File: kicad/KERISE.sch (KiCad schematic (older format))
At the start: 5 parts, among them SW1 RESET, U1 ESP32-PICO-D4

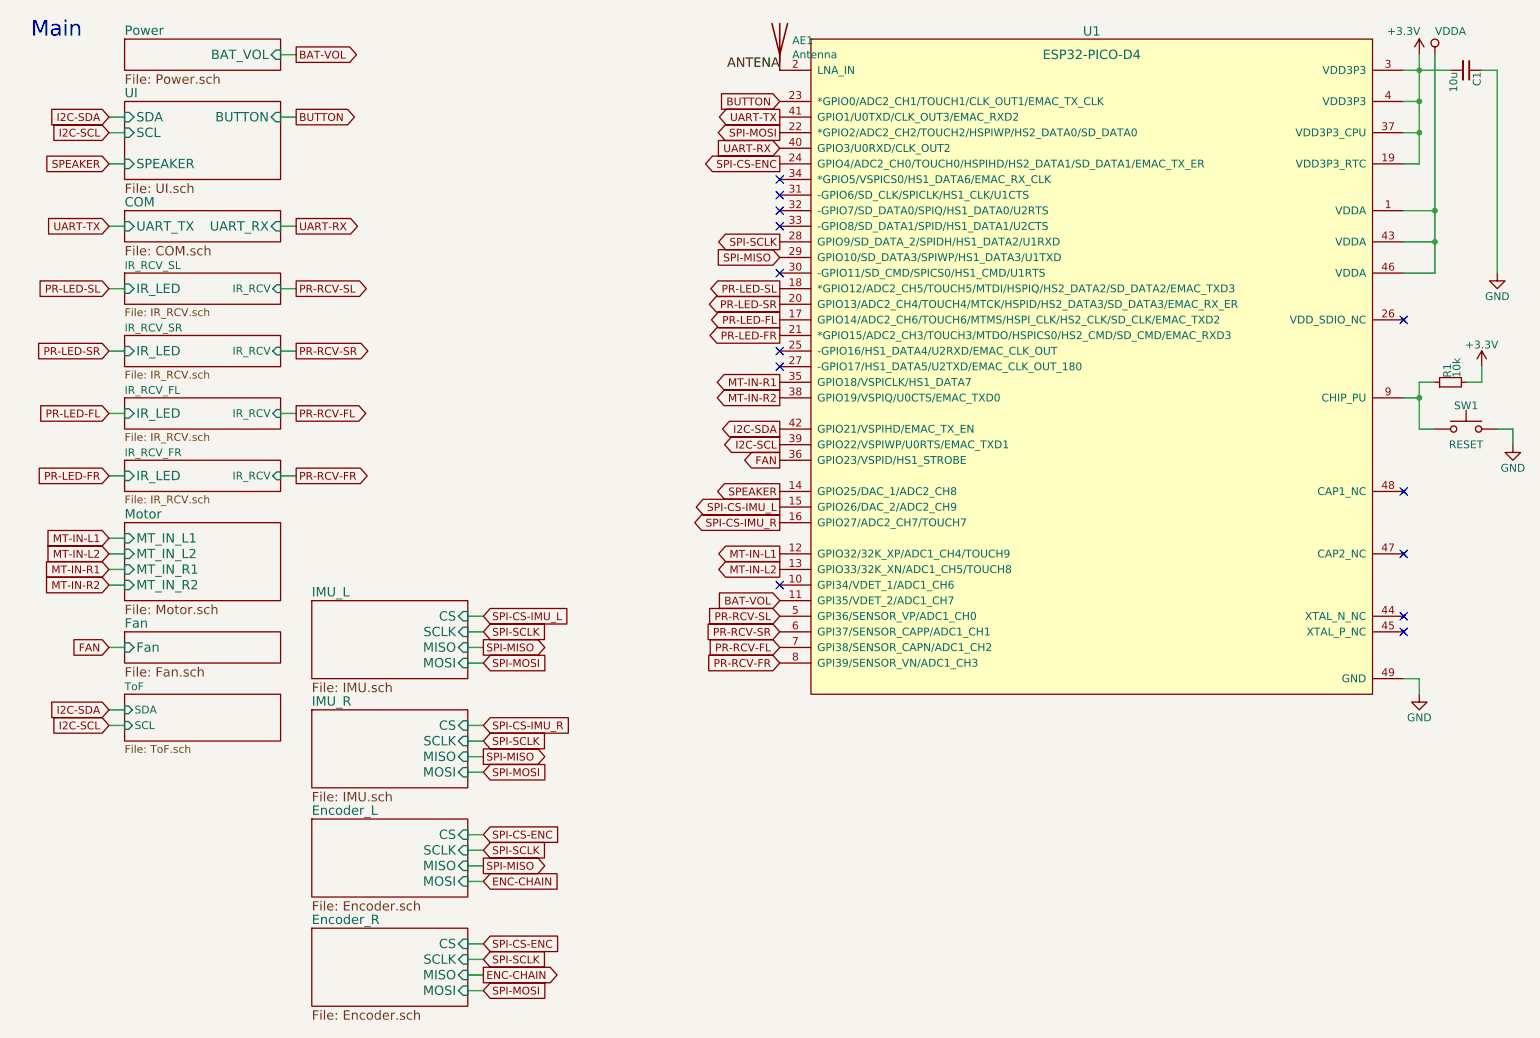
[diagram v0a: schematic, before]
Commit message: 部品を配置
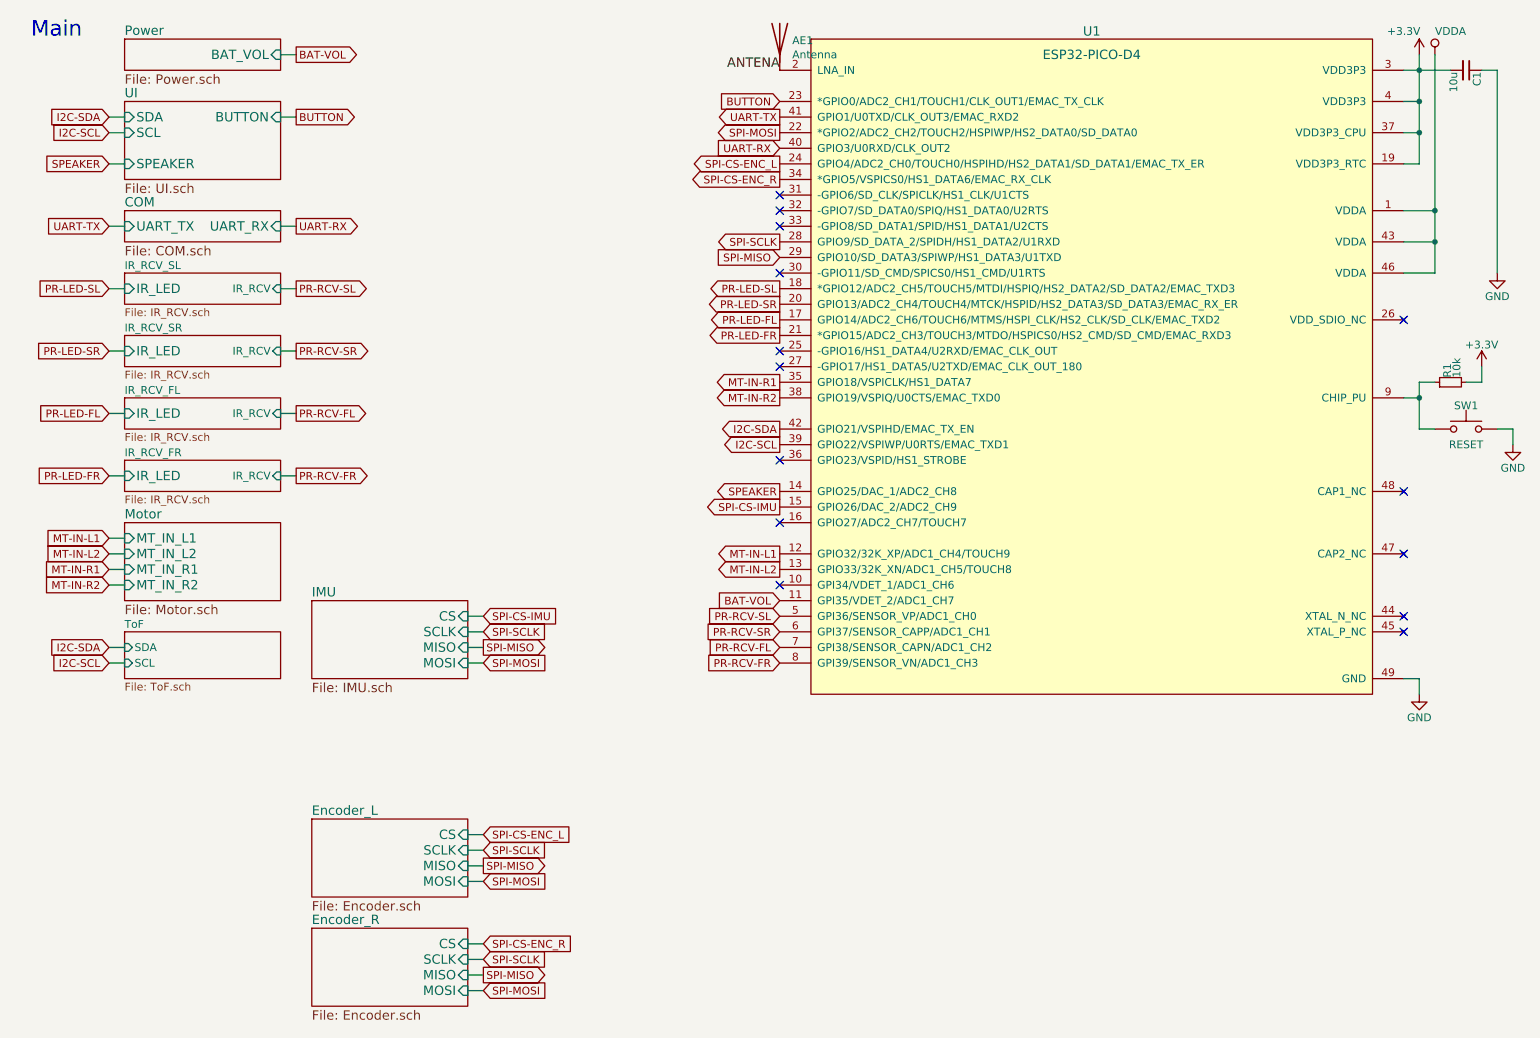
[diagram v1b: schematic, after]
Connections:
- net SPI-CS-ENC_R: now reaches U1.34 (*GPIO5/VSPICS0/HS1_DATA6/EMAC_RX_CLK)
- net FAN: no longer names the net of U1.36 (GPIO23/VSPID/HS1_STROBE)
- net SPI-CS-ENC renamed SPI-CS-ENC_L
- net SPI-CS-IMU_L renamed SPI-CS-IMU
- net SPI-CS-IMU_R: no longer names the net of U1.16 (GPIO27/ADC2_CH7/TOUCH7)
- no-connect marks 13 -> 14
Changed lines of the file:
@@
 EESchema Schematic File Version 4
 LIBS:KERISE-cache
-EELAYER 26 0
+EELAYER 29 0
 EELAYER END
 $Descr A4 11693 8268
 encoding utf-8
-Sheet 1 15
+Sheet 1 13
 Title ""
 Date ""
@@
 F3 "UART_TX" I L 1400 2000 60
 $EndSheet
-$Sheet
-S 1400 4600 1000 200
-U 58AB634E
-F0 "Fan" 60
-F1 "Fan.sch" 60
-F2 "Fan" I L 1400 4700 60
-$EndSheet
-Text GLabel 1300 4700 0    50   Input ~ 0
-FAN
-Text GLabel 5600 3500 0    50   Output ~ 0
-FAN
 Text GLabel 5600 3700 0    50   Output ~ 0
 SPEAKER
@@
 SPI-MOSI
 Text GLabel 3700 5900 2    50   Input ~ 0
-SPI-CS-ENC
+SPI-CS-ENC_L
 Text GLabel 3700 6600 2    50   Input ~ 0
-SPI-CS-ENC
+SPI-CS-ENC_R
 Text GLabel 3700 6700 2    50   Input ~ 0
 SPI-SCLK
-$Sheet
-S 2600 5100 1000 500
-U 57CC33F6
-F0 "IMU_R" 60
-F1 "IMU.sch" 60
-F2 "MISO" I R 3600 5400 60
-F3 "MOSI" I R 3600 5500 60
-F4 "CS" I R 3600 5200 60
-F5 "SCLK" I R 3600 5300 60
-$EndSheet
-Text GLabel 3700 5300 2    50   Input ~ 0
-SPI-SCLK
-Text GLabel 3700 5200 2    50   Input ~ 0
-SPI-CS-IMU_R
-Text GLabel 3700 5400 2    50   Output ~ 0
-SPI-MISO
-Text GLabel 3700 5500 2    50   Input ~ 0
-SPI-MOSI
 Text GLabel 5600 3800 0    50   Output ~ 0
-SPI-CS-IMU_L
+SPI-CS-IMU
 Text GLabel 5600 1600 0    50   Output ~ 0
-SPI-CS-ENC
+SPI-CS-ENC_L
 Text GLabel 5600 2100 0    50   Output ~ 0
 SPI-SCLK
@@
 S 2600 4400 1000 500
 U 5A18D4D6
-F0 "IMU_L" 60
+F0 "IMU" 60
 F1 "IMU.sch" 60
 F2 "MISO" I R 3600 4700 60
@@
 SPI-SCLK
 Text GLabel 3700 4500 2    50   Input ~ 0
-SPI-CS-IMU_L
+SPI-CS-IMU
 Text GLabel 3700 4700 2    50   Output ~ 0
 SPI-MISO
 Text GLabel 3700 4800 2    50   Input ~ 0
 SPI-MOSI
-Text GLabel 5600 3900 0    50   Output ~ 0
-SPI-CS-IMU_R
 NoConn ~ 9600 2600
 NoConn ~ 5600 1800
@@
 	9700 5000 9700 4900
 Wire Wire Line
-	1300 4700 1400 4700
-Wire Wire Line
 	1300 4000 1400 4000
 Wire Wire Line
@@
 Wire Wire Line
 	3600 5900 3700 5900
-Wire Wire Line
-	3700 5500 3600 5500
-Wire Wire Line
-	3600 5400 3700 5400
-Wire Wire Line
-	3700 5300 3600 5300
-Wire Wire Line
-	3600 5200 3700 5200
 Wire Wire Line
 	2500 3200 2400 3200
@@
 	1    0    0    -1
 $EndComp
-Text GLabel 3700 6200 2    50   Input ~ 0
-ENC-CHAIN
-$Sheet
-S 1400 5000 1000 300
+$Sheet
+S 1400 4600 1000 300
 U 5C29A0B1
 F0 "ToF" 50
 F1 "ToF.sch" 50
-F2 "SDA" I L 1400 5100 50
-F3 "SCL" I L 1400 5200 50
-$EndSheet
-Text GLabel 1300 5100 0    50   Input ~ 0
+F2 "SDA" I L 1400 4700 50
+F3 "SCL" I L 1400 4800 50
+$EndSheet
+Text GLabel 1300 4700 0    50   Input ~ 0
 I2C-SDA
-Text GLabel 1300 5200 0    50   Input ~ 0
+Text GLabel 1300 4800 0    50   Input ~ 0
 I2C-SCL
 Wire Wire Line
-	1300 5100 1400 5100
-Wire Wire Line
-	1400 5200 1300 5200
-NoConn ~ 5600 1700
-Text GLabel 3700 6800 2    50   Output ~ 0
-ENC-CHAIN
+	1300 4700 1400 4700
+Wire Wire Line
+	1400 4800 1300 4800
 $Comp
 L Device:Antenna AE1
@@
 Text Label 5600 1000 2    60   ~ 0
 ANTENA
+Text GLabel 3700 6200 2    50   Input ~ 0
+SPI-MOSI
+Text GLabel 3700 6800 2    50   Output ~ 0
+SPI-MISO
+Text GLabel 5600 1700 0    50   Output ~ 0
+SPI-CS-ENC_R
+NoConn ~ 5600 3500
+NoConn ~ 5600 3900
 $EndSCHEMATC
